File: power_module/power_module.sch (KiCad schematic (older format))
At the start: 21 parts, among them J1 XT60PW-M, J2 XT60U-M, J3 JST-XH, J4 JST-XH, J5 Conn_01x06, U1 NCV51460, U2 ACS781xLRTR-100U

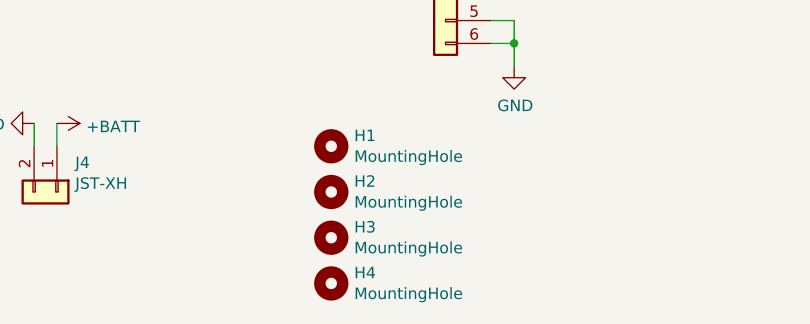
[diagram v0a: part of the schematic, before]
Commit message: first version of buck converter
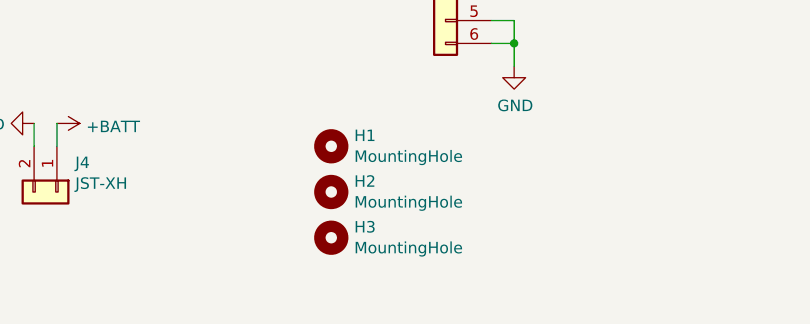
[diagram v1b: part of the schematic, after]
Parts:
- removed H4: MountingHole, hippo:MountingHole_2.7mm_M2.5_Masked, symbol Mechanical:MountingHole
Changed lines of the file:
@@
-	1    0    0    -1
-$EndComp
-$Comp
-L Mechanical:MountingHole H4
-U 1 1 6026A909
-P 4950 3850
-F 0 "H4" H 5050 3896 50  0000 L CNN
-F 1 "MountingHole" H 5050 3805 50  0000 L CNN
-F 2 "hippo:MountingHole_2.7mm_M2.5_Masked" H 4950 3850 50  0001 C CNN
-F 3 "~" H 4950 3850 50  0001 C CNN
-	1    4950 3850
 	1    0    0    -1
 $EndComp

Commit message: moved battery connector to have a safety margin
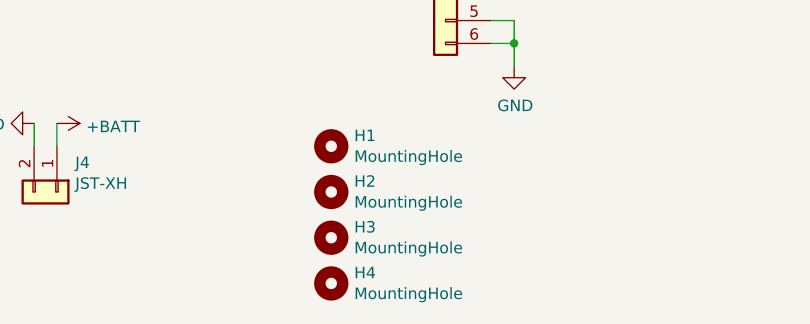
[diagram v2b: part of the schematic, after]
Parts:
- added H4: MountingHole, hippo:MountingHole_2.7mm_M2.5_Masked, symbol Mechanical:MountingHole
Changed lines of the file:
@@
 	-1   0    0    1
 $EndComp
+$Comp
+L Mechanical:MountingHole H4
+U 1 1 6030D0BC
+P 4950 3850
+F 0 "H4" H 5050 3896 50  0000 L CNN
+F 1 "MountingHole" H 5050 3805 50  0000 L CNN
+F 2 "hippo:MountingHole_2.7mm_M2.5_Masked" H 4950 3850 50  0001 C CNN
+F 3 "~" H 4950 3850 50  0001 C CNN
+	1    4950 3850
+	1    0    0    -1
+$EndComp
 $EndSCHEMATC
